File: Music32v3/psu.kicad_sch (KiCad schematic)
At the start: 7 parts, among them SW2 SW_SPDT, U2 XC6210B332MR

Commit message: PSU update
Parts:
- added C10, C8, C9: 22uf, symbol Device:C_Small
- added D1, D2: LED_Small, symbol Device:LED_Small
- added F1: Polyfuse, symbol Device:Polyfuse
- added J1: USB_C_Receptacle_USB2.0, symbol Connector:USB_C_Receptacle_USB2.0
- added R3, R4: 5.1K, symbol Device:R
- added R5, R7: 330R, symbol Device:R_Small
- added R6: 2K, symbol Device:R_Small
- added U3: SSP6206-18NR, Package_TO_SOT_SMD:SOT-23, symbol Regulator_Linear:XC6206PxxxMR
- added U4: TPD2EUSB30, Package_TO_SOT_SMD:SOT-723, symbol Power_Protection:TPD2EUSB30
- added U5: TP4057, symbol TP4057:TP4057
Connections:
- net +3V3: now also C8.1, U3.3 (VI)
- net GND: now also C10.2, C8.2, C9.2, J1.A1 (GND), J1.A12 (GND), J1.B1 (GND), J1.B12 (GND), J1.S1 (SHIELD), R3.2, R4.2, R6.2, U3.1 (GND), U4.3 (GND), U5.2 (GND)
- new net: D2.2 (A), R7.2
- new net: F1.1, J1.A4 (VBUS), J1.A9 (VBUS), J1.B4 (VBUS), J1.B9 (VBUS)
- new net: J1.B5 (CC2), R3.1
- new net: D1.2 (A), R5.2
- new net: D1.1 (K), U5.5 (STDBY)
- new net: J1.A5 (CC1), R4.1
- new net: D2.1 (K), U5.1 (CHRG)
- new net: R6.1, U5.6 (PROG)
- new net +1V8: C9.1, U3.2 (VO)
- new net BATT+: U5.3 (BAT)
- new net D+: J1.A6 (D+), J1.B6 (D+), U4.1 (D+)
- new net D-: J1.A7 (D-), J1.B7 (D-), U4.2 (D-)
- new net VBUS: C10.1, F1.2, R5.1, R7.1, U5.4 (VCC)
- no-connect marks 1 -> 3
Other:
- moved on the sheet: C4, C5, C6, C7, R2, SW2, U2

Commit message: SD card and usb and power
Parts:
- removed C4: 22uf, symbol Device:C_Small
- added BT1: Battery_Cell, Connector_JST:JST_PH_S2B-PH-SM4-TB_1x02-1MP_P2.00mm_Horizontal, symbol Device:Battery_Cell
- added C11: 1uF, symbol Device:C_Small
- added C28, C29: 1uF, Capacitor_SMD:C_0603_1608Metric, symbol Device:C_Small
- added C40: 1uF, Capacitor_SMD:C_0402_1005Metric, symbol Device:C_Small
- added D3: DSS34, Diode_SMD:D_SOD-123F, symbol Device:D_Schottky
- added F1: Polyfuse, Fuse:Fuse_0603_1608Metric, symbol Device:Polyfuse
- added Q1, Q2: CJ3134K KF, symbol Device:Q_NMOS_GSD
- added Q3: YJQD30P02A, Footprints:YJQD30P02A_DFN3.3x3.3, symbol OSSG_components_lib:YJQD30P02A
- added R22, R23: 1M, Resistor_SMD:R_0402_1005Metric, symbol Device:R_Small
- added U6: SSP61CC3602MR, Package_TO_SOT_SMD:SOT-23-3, symbol Regulator_Linear:SSP61C
- C10: value 22uf -> 1uF
- C5: value 22uf -> 4.7uF
- R5, R7: value 330R -> 2K
- SW2: value SW_SPDT -> on/off
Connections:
- net BATT+: now also C11.1, C28.1, C40.1, F1.2, Q3.1 (S2), R22.2, U6.3 (Vin)
- net GND: now also C11.2, C28.2, C29.2, C40.2, Q1.3 (D), Q2.2 (S), R23.1, U6.2 (Gnd)
- net VBUS: now also D3.2 (A), Q3.4 (G2), R23.2
- net at C5.1, R2.1, U2.1 (VIN): now also D3.1 (K), Q3.3 (S2)
- new net: Q3.5 (D2), Q3.6 (D2), Q3.7 (D2), Q3.8 (D2)
- new net: BT1.2 (+), C29.1, F1.1, Q1.1 (G)
- new net: BT1.1, Q1.2 (S)
- new net PSEN_DRIVE: Q2.3 (D), Q3.2 (G2), R22.1
- new net PSEN_GATE: Q2.1 (G), U6.1 (Out)
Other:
- note added: "1.8V regulator"
- note added: "3.3V regulator"
- note added: "3.6V trigger"
- note added: "3V-4.2V"
- note added: "400mA charge current"
- note added: "Battery"
- note added: "Battery charging"
- note added: "Power switching"
- note added: "Push-Pull"
- note added: "Reverse voltage protection"
- note added: "USB-C"
- note added: "Voltage monitor"
- moved on the sheet: C10, C5, C6, C7, C8, C9, D1, D2, F1, J1, R2, R3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

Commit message: Schematic
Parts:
- removed R2: 1M, symbol Device:R_Small
- added C28: 0.1uF, Capacitor_SMD:C_0402_1005Metric, symbol Device:C_Small
- added R22: 1M, Resistor_SMD:R_0402_1005Metric, symbol Device:R_Small
- BT1: footprint Connector_JST:JST_PH_S2B-PH-SM4-TB_1x02-1MP_P2.00mm_Horizontal -> Connector_JST:JST_GH_SM02B-GHS-TB_1x02-1MP_P1.25mm_Horizontal
- C10, C11, C5: footprint (none) -> Capacitor_SMD:C_0402_1005Metric
- C28, C29: footprint Capacitor_SMD:C_0603_1608Metric -> Capacitor_SMD:C_0402_1005Metric
- C6, C7, C8, C9: footprint (none) -> Capacitor_SMD:C_0805_2012Metric
- D1, D2: footprint (none) -> LED_SMD:LED_0603_1608Metric
- F1: footprint (none) -> Fuse:Fuse_0603_1608Metric
- J1: footprint (none) -> Music:U263-163N-4OS1735
- Q1, Q2: footprint (none) -> Package_TO_SOT_SMD:SOT-723
- Q3: footprint Footprints:YJQD30P02A_DFN3.3x3.3 -> Music:YJQD30P02A_DFN3.3x3.3
- R3, R4, R5, R6, R7: footprint (none) -> Resistor_SMD:R_0402_1005Metric
- SW2: value on/off -> Power; footprint (none) -> Button_Switch_SMD:SW_SPDT_PCM12; P/N (none) -> C145858
- U4: footprint Package_TO_SOT_SMD:SOT-723 -> Package_TO_SOT_SMD:Texas_DRT-3
- U5: footprint (none) -> Package_TO_SOT_SMD:SOT-23-6
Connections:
- net D+: now also U4.2 (D-); no longer U4.1 (D+)
- net D-: now also U4.1 (D+); no longer U4.2 (D-)
- net GND: now also SW2.1 (A), C28.2, R22.1; no longer SW2.3 (C)
- net PSEN_GATE: now also SW2.3 (C); no longer Q2.1 (G)
- net at C5.1, D3.1 (K), Q3.3 (S2)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: now also U2.3 (CE)
- net at SW2.2 (B): now also Q2.1 (G), C28.1, R22.2; no longer U2.3 (CE)
- no-connect marks 3 -> 2
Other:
- note added: "Off"
- note added: "On"
- note removed: "off"
- note removed: "on"
- moved on the sheet: C5, C6, C7, U2

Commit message: Reorganised
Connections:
- net GND: now also Q1.2 (S); no longer Q1.3 (D)
- net at BT1.1: now also Q1.3 (D); no longer Q1.2 (S)
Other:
- moved on the sheet: C8, C9, Q1, U3

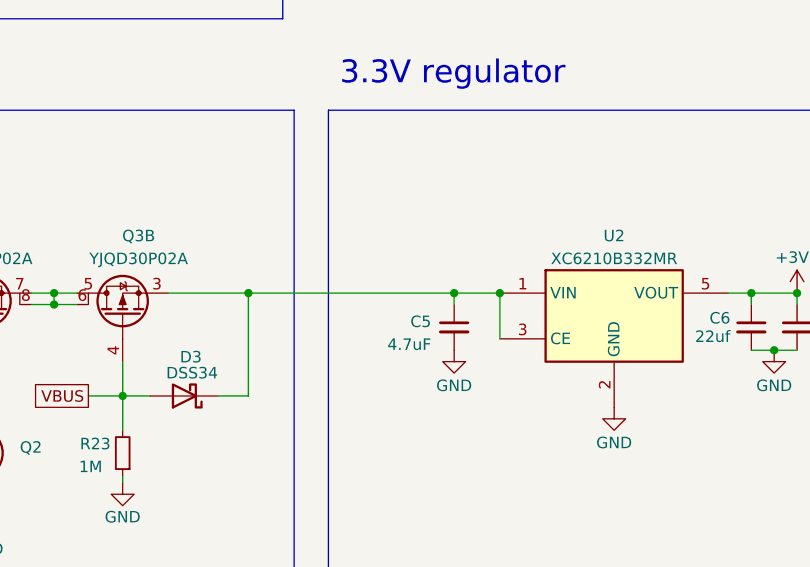
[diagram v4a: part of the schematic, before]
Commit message: PCB outline
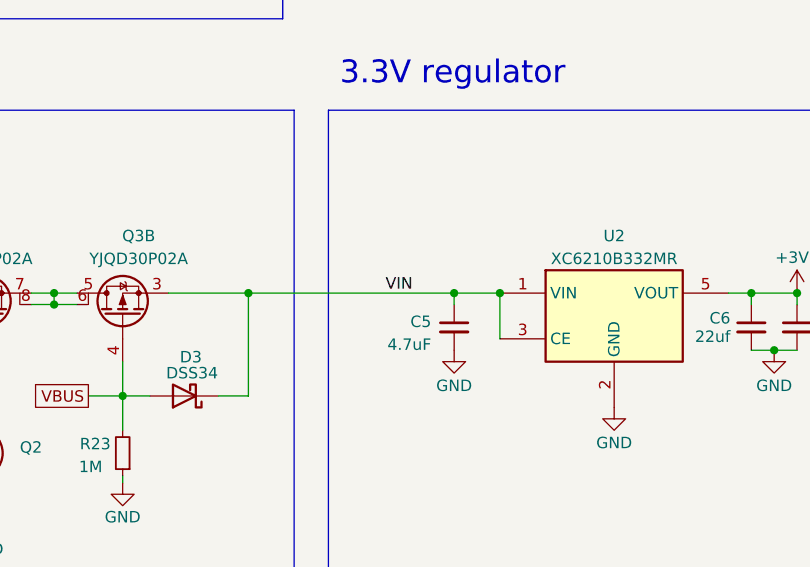
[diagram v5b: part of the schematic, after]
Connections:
- net VIN: now reaches C5.1, D3.1 (K), Q3.3 (S2), U2.1 (VIN), U2.3 (CE)
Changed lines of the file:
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@@
+    (effects (font (size 1.27 1.27)) (justify left bottom))
+  )
+  (label "VIN" (at 105.41 115.57 0) (fields_autoplaced)
     (effects (font (size 1.27 1.27)) (justify left bottom))
   )

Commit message: Board setup
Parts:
- added TP6 (x7): TestPoint, TestPoint:TestPoint_Pad_D2.0mm, symbol Connector:TestPoint
- BT1: footprint Connector_JST:JST_GH_SM02B-GHS-TB_1x02-1MP_P1.25mm_Horizontal -> Music:HCZZ0001-2
- renumbered C5 to C11, C8 to C12, C9 to C14, C6 to C15, C7 to C16, C10 to C17, C11 to C18, D1 to D2, D2 to D3, Q1 to Q2, Q2 to Q3, R4 to R21, R3 to R22, R5 to R24, R7 to R25, R6 to R26, SW2 to SW9, U5 to U10, U4 to U6, U3 to U7, U2 to U8
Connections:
- net +1V8: now also TP6.1
- net +3V3: now also TP6.1
- net BATT+: now also TP6.1
- net PSEN_GATE: now also TP6.1
- net VBUS: now also TP6.1
- net VIN: now also TP6.1
- net at C28.1, Q3.1 (G), R22.2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: now also TP6.1
